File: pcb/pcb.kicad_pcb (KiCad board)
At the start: 2 copper layers, 65.8 x 28.6 mm, 28 parts, among them IC1 LD1117-3.3V-SOT223, J1 Input, J2 Output, J3 PinHeader_01x05_P2.54mm_Horiz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, SW1 Push_Button

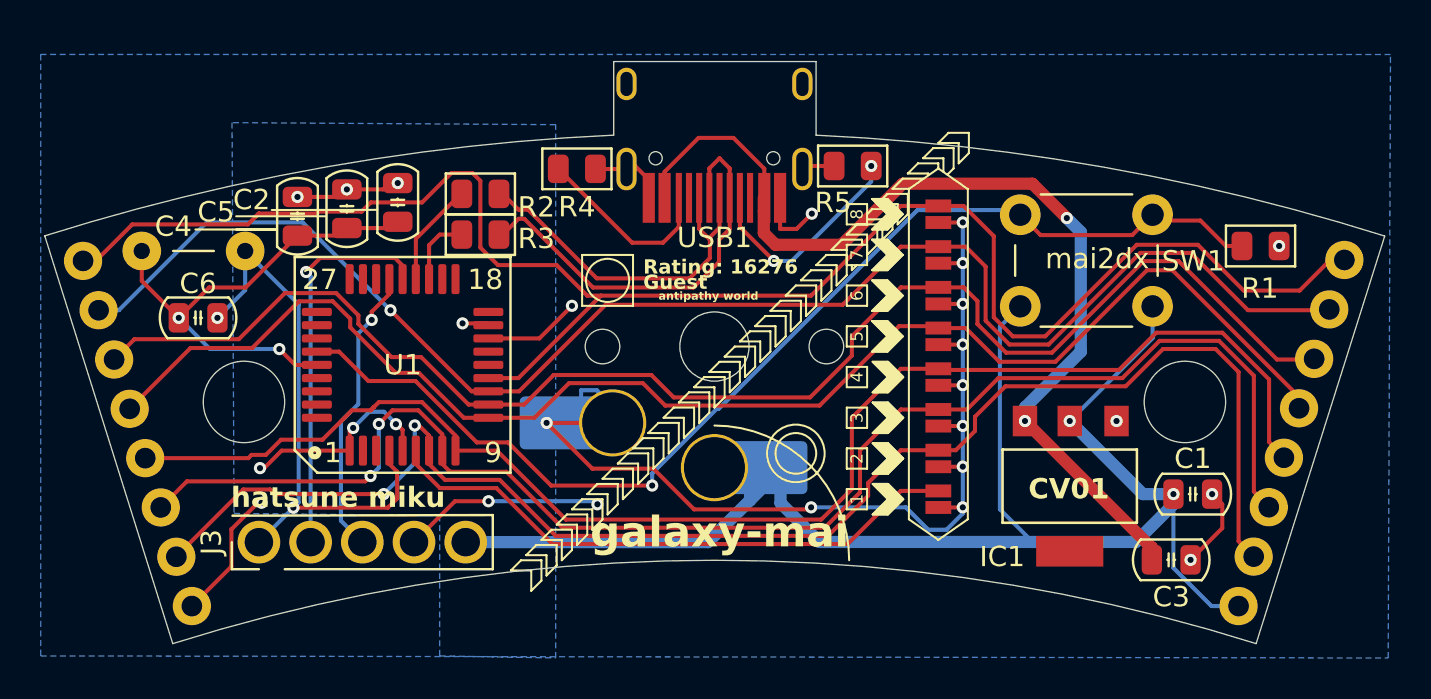
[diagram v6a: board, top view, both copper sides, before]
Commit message: revised pcb because im a dummy and put the wrong mcu size
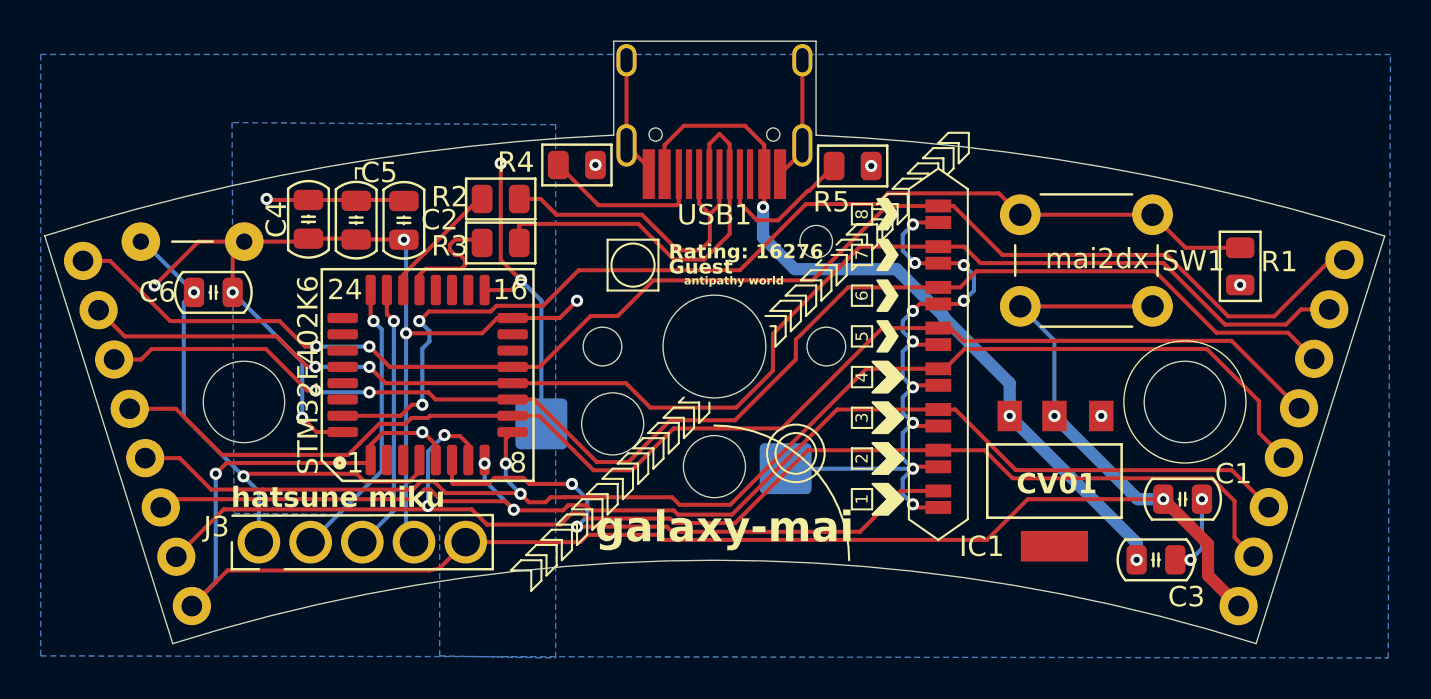
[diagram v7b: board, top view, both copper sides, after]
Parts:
- C3: value 1uF -> 100nF
- CH1: footprint PCM_marbastlib-choc:SW_choc_v1_HS_CPG135001S30_1u -> PCM_Switch_Keyboard_Hotswap_Kailh:SW_Hotswap_Kailh_Choc_V1V2; moved to F.Cu
- J1: value Input -> DNP
- J2: value Output -> DNP
- J3: value PinHeader_01x05_P2.54mm_Horizontal_SMD -> DNP
- JP1: value JUP_P5.08mm -> DNP
- STM32F402K6: renamed from U1; footprint PCM_Package_QFP_AKL:LQFP-36_7x7mm_P0.65mm -> PCM_Package_QFP_AKL:LQFP-32_7x7mm_P0.8mm
- moved C6 1.46 mm to (125.4, 97.3), turned to 180 degrees
- moved R1 1.41 mm to (175.8, 96.1), turned to 90 degrees
- moved STM32F402K6 1.33 mm to (135.9, 101.4)
- moved USB1 1.17 mm to (150.0, 83.3)
- moved R3 1.08 mm to (139.5, 94.9)
- moved R2 1.03 mm to (139.5, 92.8)
- moved C2 0.93 mm to (134.7, 93.8)
- moved IC1 0.79 mm to (166.7, 106.6)
- moved C3 0.75 mm to (171.7, 110.5)
- moved C5 0.72 mm to (132.4, 93.8)
- moved C4 0.56 mm to (130.1, 93.8)
- moved C1 0.56 mm to (173.0, 107.5)
- moved JP1 0.46 mm to (124.4, 94.8), turned to 0 degrees
- moved R4 0.19 mm to (143.2, 91.1)
- turned R5 to 180 degrees
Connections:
- J3 pad 2: /SWDIO -> /SWCLK
- J3 pad 3: /SWCLK -> /SWDIO
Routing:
- net Net-(JMP_BTN1-A): track 54.5 -> 35.3 mm
- net +3.3V: track 101.2 -> 119.0 mm, vias 10 -> 7
- net /BTN8: track 86.0 -> 70.8 mm, vias 0 -> 2
- net GND: track 53.0 -> 65.2 mm, vias 10 -> 12
- net 5V: track 49.8 -> 38.1 mm, vias 2 -> 3
- net /BTN3: track 73.4 -> 62.7 mm
- net /BTN2: track 73.7 -> 65.4 mm
- net /BTN5: track 71.6 -> 64.8 mm
- net /BTN7: track 75.3 -> 68.7 mm, vias 1 -> 2
- net /SWDIO: track 19.2 -> 13.2 mm
- net /BTN6: track 72.6 -> 67.7 mm, vias 0 -> 2
- net /BTN4: track 70.8 -> 67.2 mm, vias 0 -> 2
- net Net-(USB1-CC1): track 11.0 -> 7.51 mm, vias 2 -> 0
- net Net-(U1-PB8-BOOT0): track 55.7 -> 52.6 mm, vias 1 -> 2
- net Net-(U1-PA11): track 3.49 -> 6.40 mm
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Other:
- board size 65.8 x 28.6 mm -> 65.8 x 29.6 mm
